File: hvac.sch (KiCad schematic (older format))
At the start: 43 parts, among them IC1 ATMEGA328P-A, J1 PROGRAMMING HEADER, J2 SERIAL PORT, J3 POWER_INPUT, SW1 SPST, SW2 SPST, SW3 SPST, U1 MIC5225, U2 MOSFET_N, U3 MOSFET_N, U4 MOSFET_N

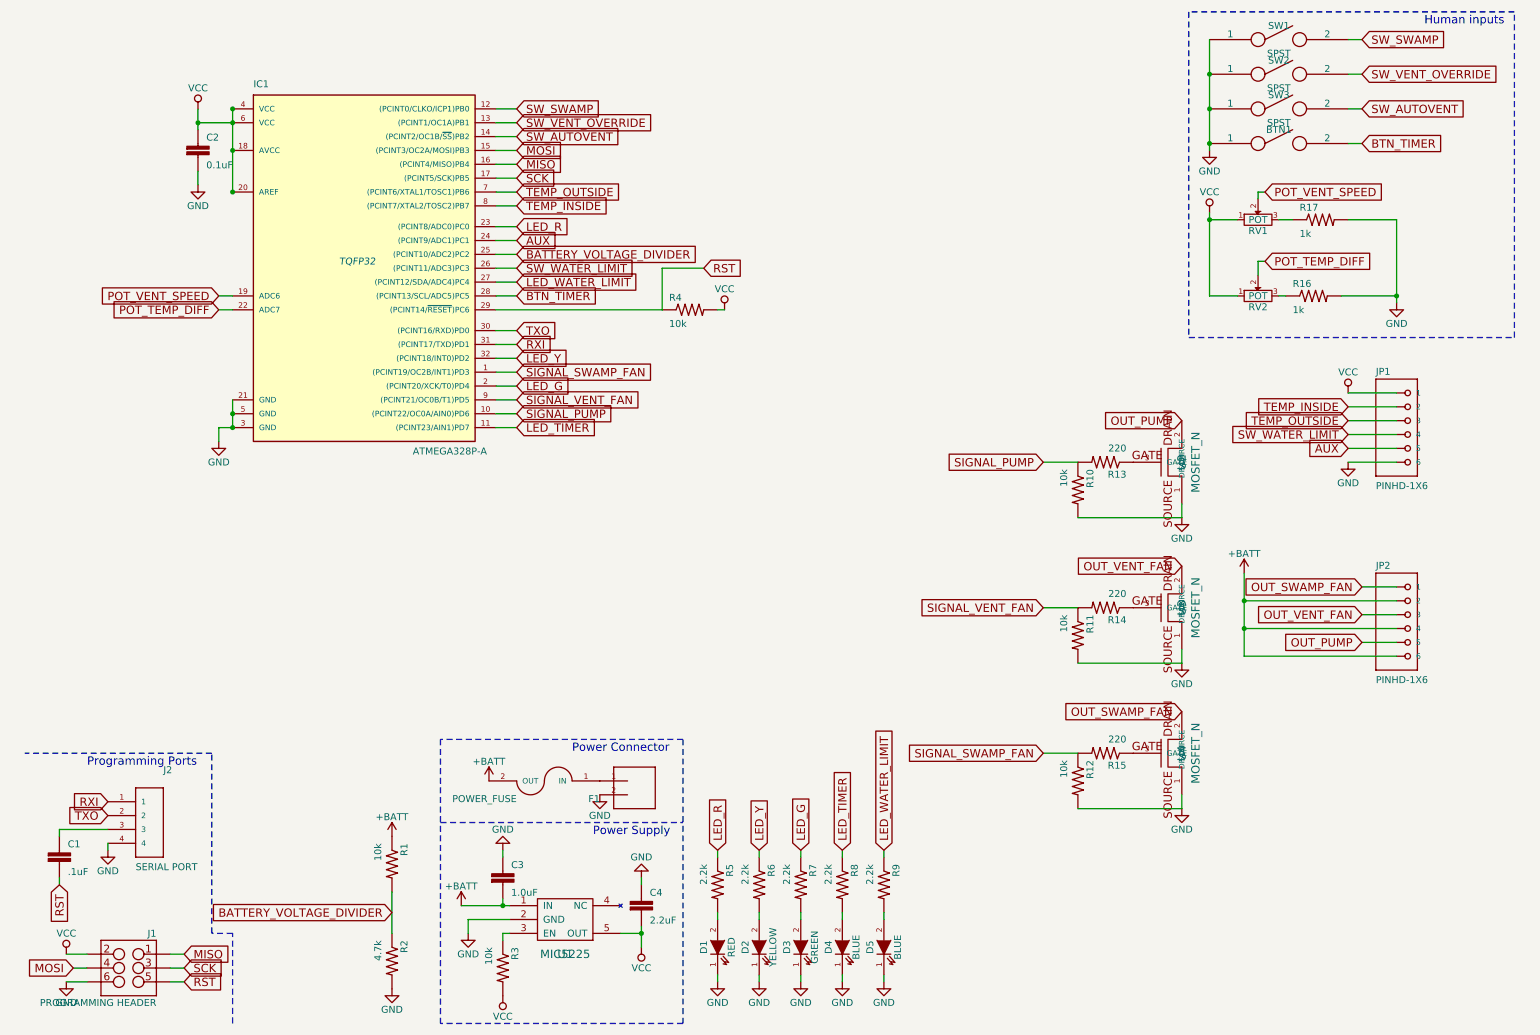
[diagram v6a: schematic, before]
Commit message: Switch to 9 pin header and provide ground/vcc for every temp sensor
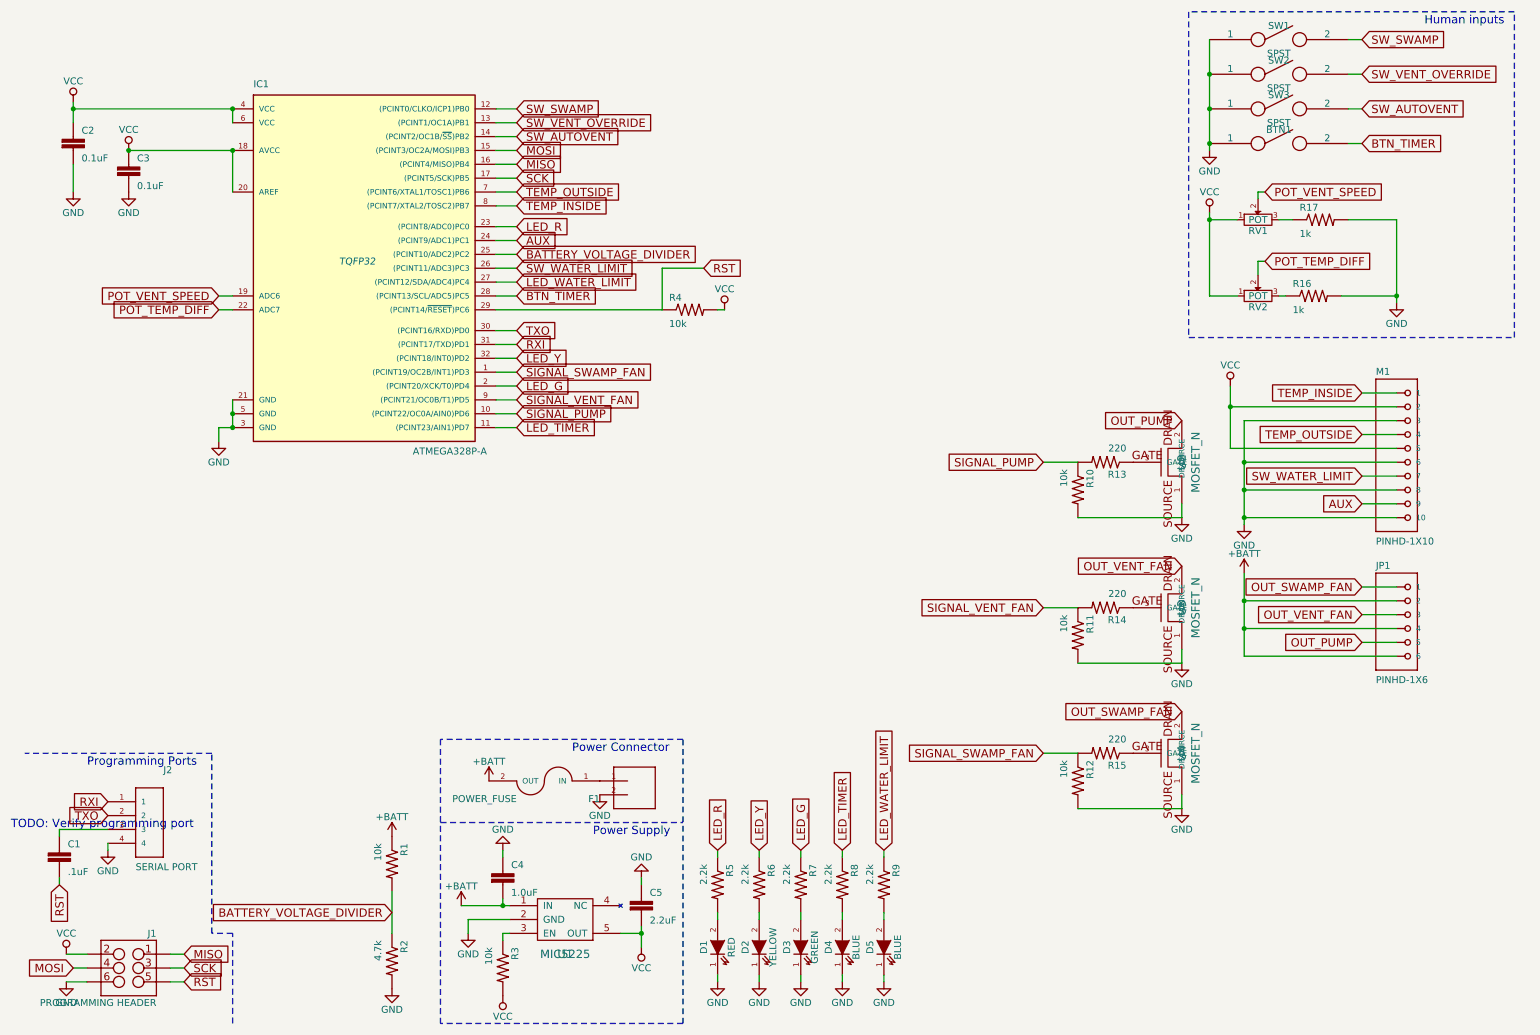
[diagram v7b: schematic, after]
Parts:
- removed JP1: PINHD-1X6, 1X06, symbol PINHD-1X6
- added C2: 0.1uF, 0603-CAP, symbol CAP0603-CAP
- added M1: PINHD-1X10, 1X10-BIG, symbol PINHD-1X10
- renumbered C2 to C3, C3 to C4, C4 to C5, JP2 to JP1
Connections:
- net AUX: now also M1.9
- net GND: now also C2.2, M1.10, M1.3, M1.6, M1.8
- net SW_WATER_LIMIT: now also M1.7
- net TEMP_INSIDE: now also M1.1
- net TEMP_OUTSIDE: now also M1.4
- net VCC: now also C2.1, M1.2, M1.5
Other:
- note added: "TODO: Verify programming port"
- moved on the sheet: C3
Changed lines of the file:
@@
 $EndComp
 $Comp
-L CAP0603-CAP C4
+L CAP0603-CAP C5
 U 1 1 590E70D3
 P 4900 7000
-F 0 "C4" H 4960 7115 50  0000 L BNN
+F 0 "C5" H 4960 7115 50  0000 L BNN
 F 1 "2.2uF" H 4960 6915 50  0000 L BNN
 F 2 "0603-CAP" H 4930 7150 20  0001 C CNN
@@
 $EndComp
 $Comp
-L CAP0603-CAP C3
+L CAP0603-CAP C4
 U 1 1 590E714A
 P 3900 6800
-F 0 "C3" H 3960 6915 50  0000 L BNN
+F 0 "C4" H 3960 6915 50  0000 L BNN
 F 1 "1.0uF" H 3960 6715 50  0000 L BNN
 F 2 "0603-CAP" H 3930 6950 20  0001 C CNN
@@
 L VCC #PWR07
 U 1 1 590E75CA
-P 1700 1200
-F 0 "#PWR07" H 1700 1050 50  0001 C CNN
-F 1 "VCC" H 1700 1350 50  0000 C CNN
-F 2 "" H 1700 1200 50  0000 C CNN
-F 3 "" H 1700 1200 50  0000 C CNN
-	1    1700 1200
-	1    0    0    -1
-$EndComp
-$Comp
-L CAP0603-CAP C2
+P 1200 1500
+F 0 "#PWR07" H 1200 1350 50  0001 C CNN
+F 1 "VCC" H 1200 1650 50  0000 C CNN
+F 2 "" H 1200 1500 50  0000 C CNN
+F 3 "" H 1200 1500 50  0000 C CNN
+	1    1200 1500
+	1    0    0    -1
+$EndComp
+$Comp
+L CAP0603-CAP C3
 U 1 1 590E75FE
-P 1700 1550
-F 0 "C2" H 1760 1665 50  0000 L BNN
-F 1 "0.1uF" H 1760 1465 50  0000 L BNN
-F 2 "0603-CAP" H 1730 1700 20  0001 C CNN
-F 3 "" H 1700 1550 60  0000 C CNN
-	1    1700 1550
+P 1200 1700
+F 0 "C3" H 1260 1815 50  0000 L BNN
+F 1 "0.1uF" H 1260 1615 50  0000 L BNN
+F 2 "0603-CAP" H 1230 1850 20  0001 C CNN
+F 3 "" H 1200 1700 60  0000 C CNN
+	1    1200 1700
 	1    0    0    -1
 $EndComp
@@
 L GND #PWR08
 U 1 1 590E76C4
-P 1700 1750
-F 0 "#PWR08" H 1700 1500 50  0001 C CNN
-F 1 "GND" H 1700 1600 50  0000 C CNN
-F 2 "" H 1700 1750 50  0000 C CNN
-F 3 "" H 1700 1750 50  0000 C CNN
-	1    1700 1750
+P 800 1800
+F 0 "#PWR08" H 800 1550 50  0001 C CNN
+F 1 "GND" H 800 1650 50  0000 C CNN
+F 2 "" H 800 1800 50  0000 C CNN
+F 3 "" H 800 1800 50  0000 C CNN
+	1    800  1800
 	1    0    0    -1
 $EndComp
@@
 Connection ~ 3900 6950
 Wire Wire Line
-	1950 1200 1950 1800
-Connection ~ 1950 1300
-Connection ~ 1950 1500
-Connection ~ 1950 1800
-Connection ~ 1950 1200
-Wire Wire Line
 	1950 3300 1950 3500
 Wire Wire Line
@@
 Text GLabel 6350 6550 1    60   Input ~ 0
 LED_TIMER
-Wire Wire Line
-	1700 1300 1950 1300
-Connection ~ 1700 1300
-Wire Wire Line
-	1700 1650 1700 1750
-Wire Wire Line
-	1700 1200 1700 1350
 $Comp
 L SPST SW1
@@
 Text Notes 10550 600  0    60   ~ 0
 Human inputs
-Text GLabel 10000 3350 0    60   Input ~ 0
+Text GLabel 10100 3250 0    60   Input ~ 0
 TEMP_INSIDE
-Text GLabel 10000 3450 0    60   Input ~ 0
+Text GLabel 10100 3550 0    60   Input ~ 0
 TEMP_OUTSIDE
 $Comp
 L VCC #PWR022
 U 1 1 590F74AC
-P 10000 3250
-F 0 "#PWR022" H 10000 3100 50  0001 C CNN
-F 1 "VCC" H 10000 3400 50  0000 C CNN
-F 2 "" H 10000 3250 50  0000 C CNN
-F 3 "" H 10000 3250 50  0000 C CNN
-	1    10000 3250
+P 9150 3200
+F 0 "#PWR022" H 9150 3050 50  0001 C CNN
+F 1 "VCC" H 9150 3350 50  0000 C CNN
+F 2 "" H 9150 3200 50  0000 C CNN
+F 3 "" H 9150 3200 50  0000 C CNN
+	1    9150 3200
 	1    0    0    -1
 $EndComp
@@
 L GND #PWR027
 U 1 1 590FE215
-P 10000 3750
-F 0 "#PWR027" H 10000 3500 50  0001 C CNN
-F 1 "GND" H 10000 3600 50  0000 C CNN
-F 2 "" H 10000 3750 50  0000 C CNN
-F 3 "" H 10000 3750 50  0000 C CNN
-	1    10000 3750
-	1    0    0    -1
-$EndComp
-Text GLabel 10000 3550 0    60   Input ~ 0
+P 9250 4200
+F 0 "#PWR027" H 9250 3950 50  0001 C CNN
+F 1 "GND" H 9250 4050 50  0000 C CNN
+F 2 "" H 9250 4200 50  0000 C CNN
+F 3 "" H 9250 4200 50  0000 C CNN
+	1    9250 4200
+	1    0    0    -1
+$EndComp
+Text GLabel 10100 3850 0    60   Input ~ 0
 SW_WATER_LIMIT
 Text GLabel 7800 4800 0    60   Input ~ 0
@@
 OUT_PUMP
 $Comp
-L PINHD-1X6 JP2
+L PINHD-1X6 JP1
 U 1 1 590FEE3F
 P 10450 4950
-F 0 "JP2" H 10200 5375 50  0000 L BNN
+F 0 "JP1" H 10200 5375 50  0000 L BNN
 F 1 "PINHD-1X6" H 10200 4550 50  0000 L BNN
 F 2 "1X06" H 10480 5100 20  0001 C CNN
@@
 Wire Wire Line
 	8800 5200 8050 5200
-$Comp
-L PINHD-1X6 JP1
-U 1 1 5910D38E
-P 10450 3550
-F 0 "JP1" H 10200 3975 50  0000 L BNN
-F 1 "PINHD-1X6" H 10200 3150 50  0000 L BNN
-F 2 "1X06" H 10480 3700 20  0001 C CNN
-F 3 "" H 10450 3550 60  0000 C CNN
-	1    10450 3550
-	1    0    0    -1
-$EndComp
 Text GLabel 4000 2150 2    60   Input ~ 0
 AUX
@@
 	4000 2150 3850 2150
 Wire Wire Line
-	10000 3750 10350 3750
-Wire Wire Line
-	10350 3650 10000 3650
-Text GLabel 10000 3650 0    60   Input ~ 0
+	9250 3750 10350 3750
+Wire Wire Line
+	9150 3650 10350 3650
+Text GLabel 10100 4050 0    60   Input ~ 0
 AUX
-Wire Wire Line
-	10000 3550 10350 3550
-Wire Wire Line
-	10350 3450 10000 3450
-Wire Wire Line
-	10000 3350 10350 3350
-Wire Wire Line
-	10350 3250 10000 3250
+Text Notes 350  6400 0    60   ~ 0
+TODO: Verify programming port
+$Comp
+L PINHD-1X10 M1
+U 1 1 5910F906
+P 10450 3650
+F 0 "M1" H 10200 4175 50  0000 L BNN
+F 1 "PINHD-1X10" H 10200 2950 50  0000 L BNN
+F 2 "1X10-BIG" H 10480 3800 20  0001 C CNN
+F 3 "" H 10450 3650 60  0000 C CNN
+	1    10450 3650
+	1    0    0    -1
+$EndComp
+Wire Wire Line
+	9150 3200 9150 3650
+Wire Wire Line
+	9150 3350 10350 3350
+Wire Wire Line
+	9250 3450 9250 4200
+Wire Wire Line
+	9250 3450 10350 3450
+Connection ~ 9250 3750
+Connection ~ 9150 3350
+Wire Wire Line
+	10350 3950 9250 3950
+Connection ~ 9250 3950
+Wire Wire Line
+	9250 4150 10350 4150
+Connection ~ 9250 4150
+Wire Wire Line
+	10100 4050 10350 4050
+Wire Wire Line
+	10100 3850 10350 3850
+Wire Wire Line
+	10350 3550 10100 3550
+Wire Wire Line
+	10100 3250 10350 3250
+$Comp
+L CAP0603-CAP C2
+U 1 1 5911190A
+P 800 1500
+F 0 "C2" H 860 1615 50  0000 L BNN
+F 1 "0.1uF" H 860 1415 50  0000 L BNN
+F 2 "0603-CAP" H 830 1650 20  0001 C CNN
+F 3 "" H 800 1500 60  0000 C CNN
+	1    800  1500
+	1    0    0    -1
+$EndComp
+$Comp
+L VCC #PWR032
+U 1 1 59112013
+P 800 1150
+F 0 "#PWR032" H 800 1000 50  0001 C CNN
+F 1 "VCC" H 800 1300 50  0000 C CNN
+F 2 "" H 800 1150 50  0000 C CNN
+F 3 "" H 800 1150 50  0000 C CNN
+	1    800  1150
+	1    0    0    -1
+$EndComp
+$Comp
+L GND #PWR033
+U 1 1 59112187
+P 1200 1800
+F 0 "#PWR033" H 1200 1550 50  0001 C CNN
+F 1 "GND" H 1200 1650 50  0000 C CNN
+F 2 "" H 1200 1800 50  0000 C CNN
+F 3 "" H 1200 1800 50  0000 C CNN
+	1    1200 1800
+	1    0    0    -1
+$EndComp
+Wire Wire Line
+	800  1600 800  1800
+Wire Wire Line
+	800  1300 800  1150
+Wire Wire Line
+	1950 1500 1950 1800
+Wire Wire Line
+	1950 1300 1950 1200
+Wire Wire Line
+	1950 1200 800  1200
+Connection ~ 800  1200
+Connection ~ 1950 1500
+Connection ~ 1950 1200
+Connection ~ 1200 1500
+Wire Wire Line
+	1200 1500 1950 1500
 $EndSCHEMATC
